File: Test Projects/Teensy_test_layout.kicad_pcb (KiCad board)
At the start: 2 copper layers, 203.2 x 101.6 mm, 106 parts, among them P1 CONN_01X02, P10 CONN_01X08, P11 CONN_01X08, P12 COLUMNS, P13 CONN_01X08, P14 CONN_01X08, P15 CONN_01X08, P16 CONN_01X08, P17 CONN_01X08, P18 CONN_01X08, P19 CONN_01X08, P2 CONN_01X07, P20 CONN_01X08, P3 CONN_01X08, P4 CONN_01X08, P5 CONN_01X08, P6 CONN_01X08, P7 ROWS, P8 CONN_01X08, P9 CONN_01X08, U1 LDO-adj-4term, U10 SF-4052, U11 SF-4052, U12 SF-4052, U13 SF-4052, U14 SF-4052, U15 SF-4052, U16 SF-4052, U17 SF-4052, U18 SF-74HC595, U19 SF-74HC595, U2 Teensy_3.2, U20 SF-74HC595, U21 SF-74HC595, U22 SF-74HC595, U23 SF-74HC595, U24 SF-74HC595, U25 SF-74HC595, U26 SF-74HC595, U27 SF-74HC595, U3 LDO-adj-4term, U4 SGTL5000, U5 SF-MicroSD-12term, U6 LDO-adj-4term, U7 2N168, U8 SF-4052, U9 SF-4052

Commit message: Tested a few layout sections
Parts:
- removed JACK1: TRS_6term, SparkFun-Footprints:SF-Neutrik-Jack-6-term
- moved C12 16.1 mm to (85.7, 131.7), turned to 270 degrees
- moved R5 15.0 mm to (130.5, 77.1)
- moved C10 15.0 mm to (130.5, 73.3)
- moved C9 15.0 mm to (128.0, 73.3)
- moved JMP4 15.0 mm to (133.9, 64.4)
- moved JMP1 15.0 mm to (114.4, 86.0)
- moved JMP2 15.0 mm to (114.4, 79.6)
- moved R6 15.0 mm to (122.9, 84.7)
- moved R7 15.0 mm to (119.1, 84.7)
- moved C11 15.0 mm to (125.2, 65.6)
- moved C8 15.0 mm to (122.9, 78.3)
- moved C7 15.0 mm to (115.3, 72.0)
- moved JMP3 15.0 mm to (128.8, 79.6)
- moved U4 15.0 mm to (122.0, 72.4)
- moved U16 14.8 mm to (193.5, 76.7)
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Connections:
- net Net-(C1-Pad1) renamed /page1/Bulk_IN
- U10 pad 13: (no net) -> KOUT5
- U10 pad 3: (no net) -> KOUT6
- U11 pad 13: (no net) -> KOUT7
- U11 pad 3: (no net) -> KOUT8
- U16 pad 1: (no net) -> KOUT5
- U16 pad 11: (no net) -> KOUT4
- U16 pad 12: (no net) -> KOUT1
- U16 pad 14: (no net) -> KOUT2
- U16 pad 15: (no net) -> KOUT3
- U16 pad 2: (no net) -> KOUT7
- U16 pad 4: (no net) -> KOUT8
- U16 pad 5: (no net) -> KOUT6
- U18 pad 14: BSER -> LEDSER
- U2 pad 28: (no net) -> BCLK
- U2 pad 29: BCLK -> (no net)
- U2 pad 31: (no net) -> LEDSER
- U8 pad 13: (no net) -> KOUT1
- U8 pad 3: (no net) -> KOUT2
- U9 pad 13: (no net) -> KOUT3
- U9 pad 3: (no net) -> KOUT4
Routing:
- net LEDSCLK: track 0.00 -> 102.9 mm, vias 0 -> 8
- net LEDLATCH: track 0.00 -> 101.0 mm, vias 0 -> 8
- net LEDOE: track 0.00 -> 99.2 mm, vias 0 -> 8
- net B: track 0.00 -> 62.6 mm, vias 0 -> 5
- net A: track 0.00 -> 58.4 mm, vias 0 -> 5
- net KOUT8: track 0.00 -> 58.2 mm, vias 0 -> 2
- net KOUT7: track 0.00 -> 53.8 mm, vias 0 -> 2
- net KOUT6: track 0.00 -> 44.3 mm, vias 0 -> 2
- net KOUT5: track 0.00 -> 41.6 mm, vias 0 -> 2
- net KOUT1: track 0.00 -> 30.2 mm, vias 0 -> 2
- net K17: track 0.00 -> 27.1 mm
- net KOUT2: track 0.00 -> 26.8 mm, vias 0 -> 2
- net K1: track 0.00 -> 26.4 mm
- net K4: track 0.00 -> 23.7 mm, vias 0 -> 2
- net K20: track 0.00 -> 22.9 mm, vias 0 -> 1
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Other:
- net class Default: clearance 0.2 -> 0.1778; trace_width 0.25 -> 0.1778; via_dia 0.6 -> 0.635; via_drill 0.4 -> 0.381
- net class JackLine added: clearance 0.3048, trace_width 0.3048, via_dia 0.635, via_drill 0.381
- net class Power added: clearance 0.254, trace_width 0.4064, via_dia 0.635, via_drill 0.381
- net class Signal added: clearance 0.254, trace_width 0.2032, via_dia 0.635, via_drill 0.381
- rule trace_clearance: 0.2 -> 0.1778
- rule trace_min: 0.2 -> 0.1778
- rule via_min_drill: 0.3 -> 0.381
- rule via_min_size: 0.4 -> 0.508

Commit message: Continued proto 1 layout
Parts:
- added C36: C, Capacitors_Tantalum_SMD:TantalC_SizeB_EIA-3528_Reflow, F.Cu at (176.3, 87.6)
- added P21: CONN_01X03, Pin_Headers:Pin_Header_Straight_1x03, F.Cu at (153.7, 90.2)
- added P2101: CONN_01X05, Pin_Headers:Pin_Header_Straight_1x05, F.Cu at (154.9, 69.8)
- added P211: CONN_01X05, Pin_Headers:Pin_Header_Straight_1x05, F.Cu at (132.1, 69.8)
- added P211: CONN_01X06, Pin_Headers:Pin_Header_Straight_1x06, F.Cu at (152.4, 63.5)
- added P211: CONN_01X06, Pin_Headers:Pin_Header_Straight_1x06, F.Cu at (172.7, 63.5)
- added P2111: CONN_01X05, Pin_Headers:Pin_Header_Straight_1x05, F.Cu at (157.5, 69.8)
- added P2121: CONN_01X05, Pin_Headers:Pin_Header_Straight_1x05, F.Cu at (160.0, 69.8)
- added P2131: CONN_01X05, Pin_Headers:Pin_Header_Straight_1x05, F.Cu at (162.6, 69.8)
- added P2141: CONN_01X05, Pin_Headers:Pin_Header_Straight_1x05, F.Cu at (165.1, 69.8)
- added P2151: CONN_01X05, Pin_Headers:Pin_Header_Straight_1x05, F.Cu at (167.6, 69.8)
- added P2161: CONN_01X05, Pin_Headers:Pin_Header_Straight_1x05, F.Cu at (170.2, 69.8)
- added P2171: CONN_01X05, Pin_Headers:Pin_Header_Straight_1x05, F.Cu at (172.7, 69.8)
- added P2181: CONN_01X05, Pin_Headers:Pin_Header_Straight_1x05, F.Cu at (175.3, 69.8)
- added P2191: CONN_01X05, Pin_Headers:Pin_Header_Straight_1x05, F.Cu at (177.8, 69.8)
- added P22: CONN_01X05, Pin_Headers:Pin_Header_Straight_1x05, F.Cu at (66.0, 95.2)
- added P2201: CONN_01X05, Pin_Headers:Pin_Header_Straight_1x05, F.Cu at (180.3, 69.8)
- added P221: CONN_01X05, Pin_Headers:Pin_Header_Straight_1x05, F.Cu at (134.6, 69.8)
- added P2211: CONN_01X05, Pin_Headers:Pin_Header_Straight_1x05, F.Cu at (182.9, 69.8)
- added P2221: CONN_01X05, Pin_Headers:Pin_Header_Straight_1x05, F.Cu at (185.4, 69.8)
- added P2231: CONN_01X05, Pin_Headers:Pin_Header_Straight_1x05, F.Cu at (188.0, 74.9)
- added P2241: CONN_01X05, Pin_Headers:Pin_Header_Straight_1x05, F.Cu at (188.0, 72.4)
- added P2251: CONN_01X05, Pin_Headers:Pin_Header_Straight_1x05, F.Cu at (188.0, 69.8)
- added P23: CONN_01X05, Pin_Headers:Pin_Header_Straight_1x05, F.Cu at (68.6, 95.2)
- added P231: CONN_01X05, Pin_Headers:Pin_Header_Straight_1x05, F.Cu at (137.2, 69.8)
- added P24: CONN_01X05, Pin_Headers:Pin_Header_Straight_1x05, F.Cu at (71.1, 95.2)
- added P241: CONN_01X05, Pin_Headers:Pin_Header_Straight_1x05, F.Cu at (139.7, 69.8)
- added P25: CONN_01X05, Pin_Headers:Pin_Header_Straight_1x05, F.Cu at (73.7, 95.2)
- added P251: CONN_01X05, Pin_Headers:Pin_Header_Straight_1x05, F.Cu at (142.2, 69.8)
- added P26: CONN_01X05, Pin_Headers:Pin_Header_Straight_1x05, F.Cu at (76.2, 95.2)
- added P261: CONN_01X05, Pin_Headers:Pin_Header_Straight_1x05, F.Cu at (144.8, 69.8)
- added P27: CONN_01X06, Pin_Headers:Pin_Header_Straight_1x06, F.Cu at (132.1, 63.5)
- added P271: CONN_01X05, Pin_Headers:Pin_Header_Straight_1x05, F.Cu at (147.3, 69.8)
- added P281: CONN_01X05, Pin_Headers:Pin_Header_Straight_1x05, F.Cu at (149.9, 69.8)
- added P291: CONN_01X05, Pin_Headers:Pin_Header_Straight_1x05, F.Cu at (152.4, 69.8)
- added P311: CONN_01X06, Pin_Headers:Pin_Header_Straight_1x06, F.Cu at (193.0, 63.5)
- added P311: CONN_01X06, Pin_Headers:Pin_Header_Straight_1x06, F.Cu at (213.4, 63.5)
- added P311: CONN_01X06, Pin_Headers:Pin_Header_Straight_1x06, F.Cu at (233.7, 63.5)
- added R11: R, Resistors_SMD:R_0603, F.Cu at (90.2, 58.4)
- added R12: R, Resistors_SMD:R_0603, F.Cu at (110.5, 58.4)
- added R13: R, Resistors_SMD:R_0603, F.Cu at (97.8, 58.4)
- added R14: R, Resistors_SMD:R_0603, F.Cu at (118.1, 58.4)
- added R15: R, Resistors_SMD:R_0603, F.Cu at (86.4, 68.6)
- added U28: SF-74x125, SparkFun-Footprints:SF-SOT-23-5, F.Cu at (94.0, 59.9)
- added U29: SF-74x125, SparkFun-Footprints:SF-SOT-23-5, F.Cu at (114.3, 59.7)
- added U30: SF-LM358, SparkFun-Footprints:SF-SOIC-8, F.Cu at (177.2, 88.3)
- P12: value COLUMNS -> COLS1
- P7: value ROWS -> COLS0
- moved JMP4 35.6 mm to (160.8, 87.6)
- moved C4 34.7 mm to (103.1, 83.8)
- moved C6 34.7 mm to (108.0, 92.7)
- moved R3 34.7 mm to (117.6, 86.4)
- moved R4 34.7 mm to (116.8, 91.4)
- moved C5 34.7 mm to (121.9, 88.9)
- moved U6 34.7 mm to (110.5, 84.4)
- moved U2 34.4 mm to (170.2, 119.4), turned to 180 degrees
- moved C10 33.5 mm to (157.2, 93.6)
- moved C9 33.5 mm to (154.6, 93.6)
- moved R5 33.5 mm to (157.2, 97.4)
- moved C11 33.5 mm to (151.9, 86.0)
- moved C8 33.5 mm to (149.6, 98.7)
- moved JMP1 33.5 mm to (141.1, 106.3)
- moved JMP2 33.5 mm to (141.1, 99.9)
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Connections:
- C26 pad 1: Net-(C26-Pad1) -> +5V
- C26 pad 2: Net-(C26-Pad2) -> GND
- C27 pad 1: Net-(C27-Pad1) -> +5V
- C27 pad 2: Net-(C27-Pad2) -> GND
- C28 pad 1: Net-(C28-Pad1) -> +5V
- C28 pad 2: Net-(C28-Pad2) -> GND
- C29 pad 1: Net-(C29-Pad1) -> +5V
- C29 pad 2: Net-(C29-Pad2) -> GND
- C30 pad 1: Net-(C30-Pad1) -> +5V
- C30 pad 2: Net-(C30-Pad2) -> GND
- C31 pad 1: Net-(C31-Pad1) -> +5V
- C31 pad 2: Net-(C31-Pad2) -> GND
- C32 pad 1: Net-(C32-Pad1) -> +5V
- C32 pad 2: Net-(C32-Pad2) -> GND
- C33 pad 1: Net-(C33-Pad1) -> +5V
- C33 pad 2: Net-(C33-Pad2) -> GND
- JACK10 pad G: (no net) -> Net-(JACK10-PadG)
- JACK10 pad R: (no net) -> Net-(JACK10-PadR)
- JACK10 pad RN: (no net) -> Net-(JACK10-PadRN)
- JACK10 pad S: (no net) -> Net-(JACK10-PadS)
- JACK10 pad T: (no net) -> Net-(JACK10-PadT)
- JACK10 pad TN: (no net) -> Net-(JACK10-PadTN)
- JACK3 pad 4: (no net) -> Net-(JACK3-Pad4)
- JACK3 pad 5: (no net) -> Net-(JACK3-Pad5)
- JACK4 pad 4: (no net) -> Net-(JACK4-Pad4)
- JACK4 pad 5: (no net) -> Net-(JACK4-Pad5)
- JACK5 pad G: (no net) -> Net-(JACK5-PadG)
- JACK5 pad R: (no net) -> Net-(JACK5-PadR)
- JACK5 pad RN: (no net) -> Net-(JACK5-PadRN)
- JACK5 pad S: (no net) -> Net-(JACK5-PadS)
- JACK5 pad T: (no net) -> Net-(JACK5-PadT)
- JACK5 pad TN: (no net) -> Net-(JACK5-PadTN)
- JACK6 pad G: (no net) -> Net-(JACK6-PadG)
- JACK6 pad R: (no net) -> Net-(JACK6-PadR)
- JACK6 pad RN: (no net) -> Net-(JACK6-PadRN)
- JACK6 pad S: (no net) -> Net-(JACK6-PadS)
- JACK6 pad T: (no net) -> Net-(JACK6-PadT)
- JACK6 pad TN: (no net) -> Net-(JACK6-PadTN)
- JACK7 pad G: (no net) -> Net-(JACK7-PadG)
- JACK7 pad R: (no net) -> Net-(JACK7-PadR)
- JACK7 pad RN: (no net) -> Net-(JACK7-PadRN)
- JACK7 pad S: (no net) -> Net-(JACK7-PadS)
- JACK7 pad T: (no net) -> Net-(JACK7-PadT)
- JACK7 pad TN: (no net) -> Net-(JACK7-PadTN)
- JACK8 pad G: (no net) -> Net-(JACK8-PadG)
- JACK8 pad R: (no net) -> Net-(JACK8-PadR)
- JACK8 pad RN: (no net) -> Net-(JACK8-PadRN)
- JACK8 pad S: (no net) -> Net-(JACK8-PadS)
- JACK8 pad T: (no net) -> Net-(JACK8-PadT)
- JACK8 pad TN: (no net) -> Net-(JACK8-PadTN)
- JACK9 pad G: (no net) -> Net-(JACK9-PadG)
- JACK9 pad R: (no net) -> Net-(JACK9-PadR)
- JACK9 pad RN: (no net) -> Net-(JACK9-PadRN)
- JACK9 pad S: (no net) -> Net-(JACK9-PadS)
- JACK9 pad T: (no net) -> Net-(JACK9-PadT)
- JACK9 pad TN: (no net) -> Net-(JACK9-PadTN)
- P2 pad 5: (no net) -> KEN
- U18 pad 16: Net-(C26-Pad1) -> +5V
- U18 pad 8: Net-(C26-Pad2) -> GND
- U19 pad 16: Net-(C27-Pad1) -> +5V
- U19 pad 8: Net-(C27-Pad2) -> GND
- U2 pad 21: (no net) -> KEN
- U20 pad 16: Net-(C28-Pad1) -> +5V
- U20 pad 8: Net-(C28-Pad2) -> GND
- U21 pad 16: Net-(C29-Pad1) -> +5V
- U21 pad 8: Net-(C29-Pad2) -> GND
- U22 pad 16: Net-(C30-Pad1) -> +5V
- U22 pad 8: Net-(C30-Pad2) -> GND
- U23 pad 16: Net-(C31-Pad1) -> +5V
- U23 pad 8: Net-(C31-Pad2) -> GND
- U24 pad 16: Net-(C32-Pad1) -> +5V
- U24 pad 8: Net-(C32-Pad2) -> GND
- U25 pad 16: Net-(C33-Pad1) -> +5V
- U25 pad 8: Net-(C33-Pad2) -> GND
- U7 pad 5: (no net) -> GND
- U7 pad 6: (no net) -> PORT-TX
- U7 pad 8: (no net) -> +5V
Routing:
- net Net-(C29-Pad2): track 1.94 -> 0.00 mm
- net GND: track 13.6 -> 15.5 mm
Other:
- board size 203.2 x 101.6 mm -> 190.5 x 101.6 mm

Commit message: Moved to 10x5 size
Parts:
- removed P2101, P211, P2111, P2121, P2131, P2141, P2151, P2161, P2171, P2181, P2191, P2201, P221, P2211, P2221, P2231, P2241, P2251, P231, P241, P251, P261, P271, P281, P291: CONN_01X05, Pin_Headers:Pin_Header_Straight_1x05
- removed P211 (x2), P311 (x3): CONN_01X06, Pin_Headers:Pin_Header_Straight_1x06
- added JACK1: DIN-5, SparkFun-Footprints:SF-DIN-5, F.Cu at (58.4, 25.4)
- added JACK11: TRS_6term, SparkFun-Footprints:SF-Neutrik-Jack-6-term, F.Cu at (264.2, 25.4)
- added P28: CONN_01X08, Pin_Headers:Pin_Header_Straight_1x08, F.Cu at (233.7, 144.8)
- added P29: CONN_01X08, Pin_Headers:Pin_Header_Straight_1x08, F.Cu at (254.0, 144.8)
- added ROWS1: CONN_01X04, Pin_Headers:Pin_Header_Straight_1x04, F.Cu at (139.7, 132.1)
- C12, C13, C14: value 10u -> C; footprint Capacitors_Tantalum_SMD:TantalC_SizeB_EIA-3528_Reflow -> Capacitors_SMD:C_1206
- C15, C36: footprint Capacitors_Tantalum_SMD:TantalC_SizeB_EIA-3528_Reflow -> Capacitors_SMD:C_0603
- C16: value 1u -> C
- C17, C18: value 1u -> C; footprint Capacitors_SMD:C_0603 -> Capacitors_Tantalum_SMD:TantalC_SizeB_EIA-3528_Reflow
- C26, C27, C28: value C -> 1u
- C7, C8, C9: value C -> 10u; footprint Capacitors_SMD:C_1206 -> Capacitors_Tantalum_SMD:TantalC_SizeB_EIA-3528_Reflow
- JACK4: value DIN-5 -> TRS_6term; footprint SparkFun-Footprints:SF-DIN-5 -> SparkFun-Footprints:SF-Neutrik-Jack-6-term
- JMP1: value 2Jumper -> 3Jumper; footprint SparkFun-Footprints:SF-2way-open -> SparkFun-Footprints:SF-3way-open
- JMP3: value 3Jumper -> 2Jumper; footprint SparkFun-Footprints:SF-3way-open -> SparkFun-Footprints:SF-2way-open
- P10, P11, P5, P6, P8, P9: value CONN_01X08 -> CONN_01X06; footprint Pin_Headers:Pin_Header_Straight_1x08 -> Pin_Headers:Pin_Header_Straight_1x06
- P12: value COLS1 -> CONN_01X06; footprint Pin_Headers:Pin_Header_Straight_1x08 -> Pin_Headers:Pin_Header_Straight_1x06
- P2: value CONN_01X07 -> CONN_01X03; footprint Pin_Headers:Pin_Header_Straight_1x07 -> Pin_Headers:Pin_Header_Straight_1x03
- P21: value CONN_01X03 -> CONN_01X07; footprint Pin_Headers:Pin_Header_Straight_1x03 -> Pin_Headers:Pin_Header_Straight_1x07
- P22, P23, P24, P25, P26: value CONN_01X05 -> CONN_01X08; footprint Pin_Headers:Pin_Header_Straight_1x05 -> Pin_Headers:Pin_Header_Straight_1x08
- P27: value CONN_01X06 -> CONN_01X08; footprint Pin_Headers:Pin_Header_Straight_1x06 -> Pin_Headers:Pin_Header_Straight_1x08
- P3: value CONN_01X08 -> COLS0
- P4: value CONN_01X08 -> COLS1
- P7: value COLS0 -> CONN_01X06; footprint Pin_Headers:Pin_Header_Straight_1x08 -> Pin_Headers:Pin_Header_Straight_1x06
- R3: value 11.5K -> 11.3K
- R4: value 18.7K -> 34K
- R5: value 1 -> 11.5K
- R6: value 2.2K -> 18.7K
- R7: value 2.2K -> 1
- R8: value 11.3K -> 2.2K
- R9: value 34K -> 2.2K
- U10, U9: value SF-4052 -> SF-74x125; footprint SparkFun-Footprints:SF-SOIC-16 -> SparkFun-Footprints:SF-SOT-23-5
- U11: value SF-4052 -> 2N168; footprint SparkFun-Footprints:SF-SOIC-16 -> SparkFun-Footprints:SF-SMD-8
- U12: value SF-4052 -> SF-LM358; footprint SparkFun-Footprints:SF-SOIC-16 -> SparkFun-Footprints:SF-SOIC-8
- U18, U19, U20, U21, U22: value SF-74HC595 -> SF-4052
- U2: value Teensy_3.2 -> LDO-adj-4term; footprint teensy footprints:Teensy_3.2_Route -> SparkFun-Footprints:SF-SOT-223
- U28, U29: value SF-74x125 -> SF-74HC595; footprint SparkFun-Footprints:SF-SOT-23-5 -> SparkFun-Footprints:SF-SOIC-16
- U3: value LDO-adj-4term -> Teensy_3.2; footprint SparkFun-Footprints:SF-SOT-223 -> teensy footprints:Teensy_3.2_Route
- U30: value SF-LM358 -> SF-74HC595; footprint SparkFun-Footprints:SF-SOIC-8 -> SparkFun-Footprints:SF-SOIC-16
- U4: value SGTL5000 -> LDO-adj-4term; footprint SparkFun-Footprints:SF-QFN-32-NXP-SGTL5000 -> SparkFun-Footprints:SF-SOT-223
- U5: value SF-MicroSD-12term -> SGTL5000; footprint SparkFun-Footprints:SF-MICRO-SD -> SparkFun-Footprints:SF-QFN-32-NXP-SGTL5000
- U6: value LDO-adj-4term -> SF-MicroSD-12term; footprint SparkFun-Footprints:SF-SOT-223 -> SparkFun-Footprints:SF-MICRO-SD
- U7: value 2N168 -> SF-74HC595; footprint SparkFun-Footprints:SF-SMD-8 -> SparkFun-Footprints:SF-SOIC-16
- U8: value SF-4052 -> SF-74HC595
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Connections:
- C10 pad 1: Net-(C10-Pad1) -> +3V3
- C11 pad 1: Net-(C11-Pad1) -> +1V8
- C12 pad 1: /page1/Bulk_IN -> Net-(C12-Pad1)
- C13 pad 1: +1V8 -> Net-(C12-Pad1)
- C16 pad 1: VDD -> Net-(C16-Pad1)
- C16 pad 2: GND -> Net-(C16-Pad2)
- C17 pad 1: VDD -> Net-(C17-Pad1)
- C17 pad 2: GND -> Net-(C17-Pad2)
- C18 pad 1: VDD -> GND
- C18 pad 2: GND -> +5V
- C2 pad 1: +5V -> +1V8
- C26 pad 1: +5V -> VDD
- C27 pad 1: +5V -> VDD
- C28 pad 1: +5V -> VDD
- C34 pad 1: Net-(C34-Pad1) -> +5V
- C34 pad 2: Net-(C34-Pad2) -> GND
- C35 pad 1: Net-(C35-Pad1) -> +5V
- C35 pad 2: Net-(C35-Pad2) -> GND
- C36 pad 1: GND -> +5V
- C36 pad 2: +5V -> GND
- C5 pad 1: Net-(C5-Pad1) -> +5V
- C7 pad 1: +3V3 -> /page1/Bulk_IN
- C8 pad 1: +1V8 -> Net-(C8-Pad1)
- C9 pad 1: Net-(C10-Pad1) -> Net-(C9-Pad1)
- JACK2 pad 4: Net-(C15-Pad2) -> Net-(JACK2-Pad4)
- JACK2 pad 5: Net-(C15-Pad1) -> Net-(JACK2-Pad5)
- JACK3 pad 4: Net-(JACK3-Pad4) -> Net-(C17-Pad2)
- JACK3 pad 5: Net-(JACK3-Pad5) -> Net-(C17-Pad1)
- JMP1 pad 1: PIN22 -> Net-(JMP1-Pad1)
- JMP1 pad 2: Net-(JMP1-Pad2) -> +3V3
- JMP2 pad 1: PIN13 -> I2S_DIN
- JMP3 pad 1: GND -> I2S_DOUT
- JMP4 pad 1: Net-(JMP4-Pad1) -> GND
- JMP4 pad 2: +3V3 -> Net-(JMP4-Pad2)
- JMP4 pad 3: Net-(C5-Pad1) -> +3V3
- P10 pad 1: K49 -> Net-(JACK9-PadT)
- P10 pad 2: K50 -> Net-(JACK9-PadR)
- P10 pad 3: K51 -> Net-(JACK9-PadS)
- P10 pad 4: K52 -> Net-(JACK9-PadG)
- P10 pad 5: K53 -> Net-(JACK9-PadRN)
- P10 pad 6: K54 -> Net-(JACK9-PadTN)
- P11 pad 1: K57 -> Net-(JACK10-PadT)
- P11 pad 2: K58 -> Net-(JACK10-PadR)
- P11 pad 3: K59 -> Net-(JACK10-PadS)
- P11 pad 4: K60 -> Net-(JACK10-PadG)
- P11 pad 5: K61 -> Net-(JACK10-PadRN)
- P11 pad 6: K62 -> Net-(JACK10-PadTN)
- P12 pad 1: Net-(P12-Pad1) -> Net-(JACK11-PadT)
- P12 pad 2: Net-(P12-Pad2) -> Net-(JACK11-PadR)
- P12 pad 3: Net-(P12-Pad3) -> Net-(JACK11-PadS)
- P12 pad 4: Net-(P12-Pad4) -> Net-(JACK11-PadG)
- P12 pad 5: Net-(P12-Pad5) -> Net-(JACK11-PadRN)
- P12 pad 6: Net-(P12-Pad6) -> Net-(JACK11-PadTN)
- P13 pad 1: Net-(P13-Pad1) -> K1
- P13 pad 2: Net-(P13-Pad2) -> K2
- P13 pad 3: Net-(P13-Pad3) -> K3
- P13 pad 4: Net-(P13-Pad4) -> K4
- P13 pad 5: Net-(P13-Pad5) -> K5
- P13 pad 6: Net-(P13-Pad6) -> K6
- P13 pad 7: Net-(P13-Pad7) -> K7
- P13 pad 8: Net-(P13-Pad8) -> K8
- P14 pad 1: Net-(P14-Pad1) -> K9
- P14 pad 2: Net-(P14-Pad2) -> K10
- P14 pad 3: Net-(P14-Pad3) -> K11
- P14 pad 4: Net-(P14-Pad4) -> K12
- P14 pad 5: Net-(P14-Pad5) -> K13
- P14 pad 6: Net-(P14-Pad6) -> K14
- P14 pad 7: Net-(P14-Pad7) -> K15
- P14 pad 8: Net-(P14-Pad8) -> K16
- P15 pad 1: Net-(P15-Pad1) -> K17
- P15 pad 2: Net-(P15-Pad2) -> K18
- P15 pad 3: Net-(P15-Pad3) -> K19
- P15 pad 4: Net-(P15-Pad4) -> K20
- P15 pad 5: Net-(P15-Pad5) -> K21
- P15 pad 6: Net-(P15-Pad6) -> K22
- P15 pad 7: Net-(P15-Pad7) -> K23
- P15 pad 8: Net-(P15-Pad8) -> K24
- P16 pad 1: Net-(P16-Pad1) -> K25
- P16 pad 2: Net-(P16-Pad2) -> K26
- P16 pad 3: Net-(P16-Pad3) -> K27
- P16 pad 4: Net-(P16-Pad4) -> K28
- P16 pad 5: Net-(P16-Pad5) -> K29
- P16 pad 6: Net-(P16-Pad6) -> K30
- P16 pad 7: Net-(P16-Pad7) -> K31
- P16 pad 8: Net-(P16-Pad8) -> K32
- P17 pad 1: Net-(P17-Pad1) -> K33
- P17 pad 2: Net-(P17-Pad2) -> K34
- P17 pad 3: Net-(P17-Pad3) -> K35
- P17 pad 4: Net-(P17-Pad4) -> K36
- P17 pad 5: Net-(P17-Pad5) -> K37
- P17 pad 6: Net-(P17-Pad6) -> K38
- P17 pad 7: Net-(P17-Pad7) -> K39
- P17 pad 8: Net-(P17-Pad8) -> K40
- P18 pad 1: Net-(P18-Pad1) -> K41
- P18 pad 2: Net-(P18-Pad2) -> K42
- P18 pad 3: Net-(P18-Pad3) -> K43
- P18 pad 4: Net-(P18-Pad4) -> K44
- P18 pad 5: Net-(P18-Pad5) -> K45
- P18 pad 6: Net-(P18-Pad6) -> K46
- P18 pad 7: Net-(P18-Pad7) -> K47
- P18 pad 8: Net-(P18-Pad8) -> K48
- P19 pad 1: Net-(P19-Pad1) -> K49
- P19 pad 2: Net-(P19-Pad2) -> K50
- P19 pad 3: Net-(P19-Pad3) -> K51
- P19 pad 4: Net-(P19-Pad4) -> K52
- P19 pad 5: Net-(P19-Pad5) -> K53
- P19 pad 6: Net-(P19-Pad6) -> K54
- P19 pad 7: Net-(P19-Pad7) -> K55
- P19 pad 8: Net-(P19-Pad8) -> K56
- P2 pad 1: KA0 -> Net-(P2-Pad1)
- P2 pad 2: KA1 -> Net-(P2-Pad2)
- P2 pad 3: KA2 -> Net-(P2-Pad3)
- P20 pad 1: Net-(P20-Pad1) -> K57
- P20 pad 2: Net-(P20-Pad2) -> K58
- P20 pad 3: Net-(P20-Pad3) -> K59
- P20 pad 4: Net-(P20-Pad4) -> K60
- P20 pad 5: Net-(P20-Pad5) -> K61
- P20 pad 6: Net-(P20-Pad6) -> K62
- P20 pad 7: Net-(P20-Pad7) -> K63
- P20 pad 8: Net-(P20-Pad8) -> K64
- P21 pad 1: Net-(P21-Pad1) -> KA0
- P21 pad 2: Net-(P21-Pad2) -> KA1
- P21 pad 3: Net-(P21-Pad3) -> KA2
- P22 pad 1: (no net) -> Net-(P22-Pad1)
- P22 pad 2: (no net) -> Net-(P22-Pad2)
- P22 pad 3: (no net) -> Net-(P22-Pad3)
- P22 pad 4: (no net) -> Net-(P22-Pad4)
- P22 pad 5: (no net) -> Net-(P22-Pad5)
- P23 pad 1: (no net) -> Net-(P23-Pad1)
- P23 pad 2: (no net) -> Net-(P23-Pad2)
- P23 pad 3: (no net) -> Net-(P23-Pad3)
- P23 pad 4: (no net) -> Net-(P23-Pad4)
- P23 pad 5: (no net) -> Net-(P23-Pad5)
- P24 pad 1: (no net) -> Net-(P24-Pad1)
- P24 pad 2: (no net) -> Net-(P24-Pad2)
- P24 pad 3: (no net) -> Net-(P24-Pad3)
- P24 pad 4: (no net) -> Net-(P24-Pad4)
- P24 pad 5: (no net) -> Net-(P24-Pad5)
- P25 pad 1: (no net) -> Net-(P25-Pad1)
- P25 pad 2: (no net) -> Net-(P25-Pad2)
- P25 pad 3: (no net) -> Net-(P25-Pad3)
- P25 pad 4: (no net) -> Net-(P25-Pad4)
- P25 pad 5: (no net) -> Net-(P25-Pad5)
- P26 pad 1: (no net) -> Net-(P26-Pad1)
- P26 pad 2: (no net) -> Net-(P26-Pad2)
- P26 pad 3: (no net) -> Net-(P26-Pad3)
- P26 pad 4: (no net) -> Net-(P26-Pad4)
- P26 pad 5: (no net) -> Net-(P26-Pad5)
- P27 pad 1: Net-(JACK5-PadRN) -> Net-(P27-Pad1)
- P27 pad 2: Net-(JACK5-PadR) -> Net-(P27-Pad2)
- P27 pad 3: Net-(JACK5-PadTN) -> Net-(P27-Pad3)
- P27 pad 4: Net-(JACK5-PadT) -> Net-(P27-Pad4)
- P27 pad 5: Net-(JACK5-PadG) -> Net-(P27-Pad5)
- P27 pad 6: Net-(JACK5-PadS) -> Net-(P27-Pad6)
- P3 pad 1: K1 -> Net-(P3-Pad1)
- P3 pad 2: K2 -> Net-(P3-Pad2)
- P3 pad 3: K3 -> Net-(P3-Pad3)
- P3 pad 4: K4 -> Net-(P3-Pad4)
- P3 pad 5: K5 -> Net-(P3-Pad5)
- P3 pad 6: K6 -> Net-(P3-Pad6)
- P3 pad 7: K7 -> Net-(P3-Pad7)
- P3 pad 8: K8 -> Net-(P3-Pad8)
- P4 pad 1: K9 -> Net-(P4-Pad1)
- P4 pad 2: K10 -> Net-(P4-Pad2)
- P4 pad 3: K11 -> Net-(P4-Pad3)
- P4 pad 4: K12 -> Net-(P4-Pad4)
- P4 pad 5: K13 -> Net-(P4-Pad5)
- P4 pad 6: K14 -> Net-(P4-Pad6)
- P4 pad 7: K15 -> Net-(P4-Pad7)
- P4 pad 8: K16 -> Net-(P4-Pad8)
- P5 pad 1: K17 -> Net-(JACK4-PadT)
- P5 pad 2: K18 -> Net-(JACK4-PadR)
- P5 pad 3: K19 -> Net-(JACK4-PadS)
- P5 pad 4: K20 -> Net-(JACK4-PadG)
- P5 pad 5: K21 -> Net-(JACK4-PadRN)
- P5 pad 6: K22 -> Net-(JACK4-PadTN)
- P6 pad 1: K25 -> Net-(JACK5-PadT)
- P6 pad 2: K26 -> Net-(JACK5-PadR)
- P6 pad 3: K27 -> Net-(JACK5-PadS)
- P6 pad 4: K28 -> Net-(JACK5-PadG)
- P6 pad 5: K29 -> Net-(JACK5-PadRN)
- P6 pad 6: K30 -> Net-(JACK5-PadTN)
- P7 pad 1: Net-(P7-Pad1) -> Net-(JACK6-PadT)
- P7 pad 2: Net-(P7-Pad2) -> Net-(JACK6-PadR)
- P7 pad 3: Net-(P7-Pad3) -> Net-(JACK6-PadS)
- P7 pad 4: Net-(P7-Pad4) -> Net-(JACK6-PadG)
- P7 pad 5: Net-(P7-Pad5) -> Net-(JACK6-PadRN)
- P7 pad 6: Net-(P7-Pad6) -> Net-(JACK6-PadTN)
- P8 pad 1: K33 -> Net-(JACK7-PadT)
- P8 pad 2: K34 -> Net-(JACK7-PadR)
- P8 pad 3: K35 -> Net-(JACK7-PadS)
- P8 pad 4: K36 -> Net-(JACK7-PadG)
- P8 pad 5: K37 -> Net-(JACK7-PadRN)
- P8 pad 6: K38 -> Net-(JACK7-PadTN)
- P9 pad 1: K41 -> Net-(JACK8-PadT)
- P9 pad 2: K42 -> Net-(JACK8-PadR)
- P9 pad 3: K43 -> Net-(JACK8-PadS)
- P9 pad 4: K44 -> Net-(JACK8-PadG)
- P9 pad 5: K45 -> Net-(JACK8-PadRN)
- P9 pad 6: K46 -> Net-(JACK8-PadTN)
- R1 pad 1: +5V -> +1V8
- R10 pad 1: Net-(C15-Pad2) -> +5V
- R10 pad 2: Net-(R10-Pad2) -> Net-(JACK1-Pad4)
- R11 pad 2: Net-(JACK3-Pad4) -> Net-(JACK2-Pad4)
- R12 pad 1: +5V -> Net-(JACK1-Pad5)
- R12 pad 2: Net-(JACK4-Pad4) -> Net-(R12-Pad2)
- R13 pad 1: Net-(JACK3-Pad5) -> Net-(JACK2-Pad5)
- R14 pad 1: Net-(JACK4-Pad5) -> Net-(C17-Pad2)
- R15 pad 2: PORT-TX -> PORT-RX
- R3 pad 1: Net-(C5-Pad1) -> +5V
- R5 pad 1: +3V3 -> Net-(C8-Pad1)
- R5 pad 2: Net-(C10-Pad1) -> Net-(C9-Pad1)
- R6 pad 1: +3V3 -> Net-(C9-Pad1)
- R6 pad 2: SCL0 -> GND
- R7 pad 2: SDA0 -> Net-(C12-Pad1)
- R8 pad 1: +1V8 -> +3V3
- R8 pad 2: Net-(C14-Pad1) -> SCL0
- R9 pad 1: Net-(C14-Pad1) -> +3V3
- R9 pad 2: GND -> SDA0
- U1 pad 1: Net-(C14-Pad1) -> Net-(C3-Pad1)
- U10 pad 1: K21 -> GND
- U10 pad 2: K23 -> PORT-TX
- U10 pad 3: KOUT6 -> GND
- U10 pad 4: K24 -> Net-(R13-Pad2)
- U10 pad 5: K22 -> +5V
- U11 pad 1: K29 -> (no net)
- U11 pad 2: K31 -> Net-(R14-Pad2)
- U11 pad 3: KOUT8 -> Net-(C17-Pad1)
- U11 pad 4: K32 -> (no net)
- U11 pad 5: K30 -> GND
- U11 pad 6: EN -> PORT-RX
- U11 pad 7: GND -> (no net)
- U11 pad 8: (no net) -> +5V
- U12 pad 1: K37 -> (no net)
- U12 pad 2: K39 -> (no net)
- U12 pad 3: KOUT10 -> (no net)
- U12 pad 4: K40 -> GND
- U12 pad 5: K38 -> (no net)
- U12 pad 6: EN -> (no net)
- U12 pad 7: GND -> (no net)
- U12 pad 8: (no net) -> +5V
- U13 pad 1: K45 -> K5
- U13 pad 11: K44 -> K4
- U13 pad 12: K41 -> K1
- U13 pad 13: KOUT11 -> KOUT1
- U13 pad 14: K42 -> K2
- U13 pad 15: K43 -> K3
- U13 pad 2: K47 -> K7
- U13 pad 3: KOUT12 -> KOUT2
- U13 pad 4: K48 -> K8
- U13 pad 5: K46 -> K6
- U14 pad 1: K53 -> K13
- U14 pad 11: K52 -> K12
- U14 pad 12: K49 -> K9
- U14 pad 13: KOUT13 -> KOUT3
- U14 pad 14: K50 -> K10
- U14 pad 15: K51 -> K11
- U14 pad 2: K55 -> K15
- U14 pad 3: KOUT14 -> KOUT4
- U14 pad 4: K56 -> K16
- U14 pad 5: K54 -> K14
- U15 pad 1: K61 -> K21
- U15 pad 11: K60 -> K20
- U15 pad 12: K57 -> K17
- U15 pad 13: KOUT15 -> KOUT5
- U15 pad 14: K58 -> K18
- U15 pad 15: K59 -> K19
- U15 pad 2: K63 -> K23
- U15 pad 3: KOUT16 -> KOUT6
- U15 pad 4: K64 -> K24
- U15 pad 5: K62 -> K22
- U16 pad 1: KOUT5 -> K29
- U16 pad 11: KOUT4 -> K28
- U16 pad 12: KOUT1 -> K25
- U16 pad 13: KA0 -> KOUT7
- U16 pad 14: KOUT2 -> K26
- U16 pad 15: KOUT3 -> K27
- U16 pad 2: KOUT7 -> K31
- U16 pad 3: KA1 -> KOUT8
- U16 pad 4: KOUT8 -> K32
- U16 pad 5: KOUT6 -> K30
- U17 pad 1: KOUT13 -> K37
- U17 pad 11: KOUT12 -> K36
- U17 pad 12: KOUT9 -> K33
- U17 pad 13: KA2 -> KOUT9
- U17 pad 14: KOUT10 -> K34
- U17 pad 15: KOUT11 -> K35
- U17 pad 2: KOUT15 -> K39
- U17 pad 3: KA3 -> KOUT10
- U17 pad 4: KOUT16 -> K40
- U17 pad 5: KOUT14 -> K38
- U18 pad 1: Net-(P13-Pad2) -> K45
- U18 pad 10: (no net) -> A
- U18 pad 11: LEDSCLK -> K44
- U18 pad 12: LEDLATCH -> K41
- U18 pad 13: LEDOE -> KOUT11
- U18 pad 14: LEDSER -> K42
- U18 pad 15: Net-(P13-Pad1) -> K43
- U18 pad 16: +5V -> (no net)
- U18 pad 2: Net-(P13-Pad3) -> K47
- U18 pad 3: Net-(P13-Pad4) -> KOUT12
- U18 pad 4: Net-(P13-Pad5) -> K48
- U18 pad 5: Net-(P13-Pad6) -> K46
- U18 pad 6: Net-(P13-Pad7) -> EN
- U18 pad 7: Net-(P13-Pad8) -> GND
- U18 pad 8: GND -> (no net)
- U18 pad 9: Net-(U18-Pad9) -> B
- U19 pad 1: Net-(P14-Pad2) -> K53
- U19 pad 10: (no net) -> A
- U19 pad 11: LEDSCLK -> K52
- U19 pad 12: LEDLATCH -> K49
- U19 pad 13: LEDOE -> KOUT13
- U19 pad 14: Net-(U18-Pad9) -> K50
- U19 pad 15: Net-(P14-Pad1) -> K51
- U19 pad 16: +5V -> (no net)
- U19 pad 2: Net-(P14-Pad3) -> K55
- U19 pad 3: Net-(P14-Pad4) -> KOUT14
- U19 pad 4: Net-(P14-Pad5) -> K56
- U19 pad 5: Net-(P14-Pad6) -> K54
- U19 pad 6: Net-(P14-Pad7) -> EN
- U19 pad 7: Net-(P14-Pad8) -> GND
- U19 pad 8: GND -> (no net)
- U19 pad 9: Net-(U19-Pad9) -> B
- U2 pad 1: (no net) -> Net-(C6-Pad1)
- U2 pad 2: (no net) -> +5V
- U2 pad 3: (no net) -> /page1/Bulk_IN
- U2 pad 4: (no net) -> +5V
- U20 pad 1: Net-(P15-Pad2) -> K61
- U20 pad 10: (no net) -> A
- U20 pad 11: LEDSCLK -> K60
- U20 pad 12: LEDLATCH -> K57
- U20 pad 13: LEDOE -> KOUT15
- U20 pad 14: Net-(U19-Pad9) -> K58
- U20 pad 15: Net-(P15-Pad1) -> K59
- U20 pad 16: +5V -> (no net)
- U20 pad 2: Net-(P15-Pad3) -> K63
- U20 pad 3: Net-(P15-Pad4) -> KOUT16
- U20 pad 4: Net-(P15-Pad5) -> K64
- U20 pad 5: Net-(P15-Pad6) -> K62
- U20 pad 6: Net-(P15-Pad7) -> EN
- U20 pad 7: Net-(P15-Pad8) -> GND
- U20 pad 8: GND -> (no net)
- U20 pad 9: Net-(U20-Pad9) -> B
- U21 pad 1: Net-(P16-Pad2) -> KOUT5
- U21 pad 10: (no net) -> A
- U21 pad 11: LEDSCLK -> KOUT4
- U21 pad 12: LEDLATCH -> KOUT1
- U21 pad 13: LEDOE -> KA0
- U21 pad 14: Net-(U20-Pad9) -> KOUT2
- U21 pad 15: Net-(P16-Pad1) -> KOUT3
- U21 pad 16: +5V -> (no net)
- U21 pad 2: Net-(P16-Pad3) -> KOUT7
- U21 pad 3: Net-(P16-Pad4) -> KA1
- U21 pad 4: Net-(P16-Pad5) -> KOUT8
- U21 pad 5: Net-(P16-Pad6) -> KOUT6
- U21 pad 6: Net-(P16-Pad7) -> EN
- U21 pad 7: Net-(P16-Pad8) -> GND
- U21 pad 8: GND -> (no net)
- U21 pad 9: Net-(U21-Pad9) -> B
- U22 pad 1: Net-(P17-Pad2) -> KOUT13
- U22 pad 10: (no net) -> A
- U22 pad 11: LEDSCLK -> KOUT12
- U22 pad 12: LEDLATCH -> KOUT9
- U22 pad 13: LEDOE -> KA2
- U22 pad 14: Net-(U21-Pad9) -> KOUT10
- U22 pad 15: Net-(P17-Pad1) -> KOUT11
- U22 pad 16: +5V -> (no net)
- U22 pad 2: Net-(P17-Pad3) -> KOUT15
- U22 pad 3: Net-(P17-Pad4) -> KA3
- U22 pad 4: Net-(P17-Pad5) -> KOUT16
- U22 pad 5: Net-(P17-Pad6) -> KOUT14
- U22 pad 6: Net-(P17-Pad7) -> EN
- U22 pad 7: Net-(P17-Pad8) -> GND
- U22 pad 8: GND -> (no net)
- U22 pad 9: Net-(U22-Pad9) -> B
- U23 pad 1: Net-(P18-Pad2) -> Net-(P22-Pad2)
- U23 pad 11: LEDSCLK -> SD_LED_SCK
- U23 pad 14: Net-(U22-Pad9) -> SD_LED_MOSI
- U23 pad 15: Net-(P18-Pad1) -> Net-(P22-Pad1)
- U23 pad 2: Net-(P18-Pad3) -> Net-(P22-Pad3)
- U23 pad 3: Net-(P18-Pad4) -> Net-(P22-Pad4)
- U23 pad 4: Net-(P18-Pad5) -> Net-(P22-Pad5)
- U23 pad 5: Net-(P18-Pad6) -> Net-(P22-Pad6)
- U23 pad 6: Net-(P18-Pad7) -> Net-(P22-Pad7)
- U23 pad 7: Net-(P18-Pad8) -> Net-(P22-Pad8)
- U24 pad 1: Net-(P19-Pad2) -> Net-(P23-Pad2)
- U24 pad 11: LEDSCLK -> SD_LED_SCK
- U24 pad 15: Net-(P19-Pad1) -> Net-(P23-Pad1)
- U24 pad 2: Net-(P19-Pad3) -> Net-(P23-Pad3)
- U24 pad 3: Net-(P19-Pad4) -> Net-(P23-Pad4)
- U24 pad 4: Net-(P19-Pad5) -> Net-(P23-Pad5)
- U24 pad 5: Net-(P19-Pad6) -> Net-(P23-Pad6)
- U24 pad 6: Net-(P19-Pad7) -> Net-(P23-Pad7)
- U24 pad 7: Net-(P19-Pad8) -> Net-(P23-Pad8)
- U25 pad 1: Net-(P20-Pad2) -> Net-(P24-Pad2)
- U25 pad 11: LEDSCLK -> SD_LED_SCK
- U25 pad 15: Net-(P20-Pad1) -> Net-(P24-Pad1)
- U25 pad 2: Net-(P20-Pad3) -> Net-(P24-Pad3)
- U25 pad 3: Net-(P20-Pad4) -> Net-(P24-Pad4)
- U25 pad 4: Net-(P20-Pad5) -> Net-(P24-Pad5)
- U25 pad 5: Net-(P20-Pad6) -> Net-(P24-Pad6)
- U25 pad 6: Net-(P20-Pad7) -> Net-(P24-Pad7)
- U25 pad 7: Net-(P20-Pad8) -> Net-(P24-Pad8)
- U25 pad 9: (no net) -> Net-(U25-Pad9)
- U26 pad 1: Net-(P7-Pad2) -> Net-(P25-Pad2)
- U26 pad 11: BCLK -> SD_LED_SCK
- U26 pad 12: BLATCH -> LEDLATCH
- U26 pad 13: BOE -> LEDOE
- U26 pad 14: BSER -> Net-(U25-Pad9)
- U26 pad 15: Net-(P7-Pad1) -> Net-(P25-Pad1)
- U26 pad 16: Net-(C34-Pad1) -> +5V
- U26 pad 2: Net-(P7-Pad3) -> Net-(P25-Pad3)
- U26 pad 3: Net-(P7-Pad4) -> Net-(P25-Pad4)
- U26 pad 4: Net-(P7-Pad5) -> Net-(P25-Pad5)
- U26 pad 5: Net-(P7-Pad6) -> Net-(P25-Pad6)
- U26 pad 6: Net-(P7-Pad7) -> Net-(P25-Pad7)
- U26 pad 7: Net-(P7-Pad8) -> Net-(P25-Pad8)
- U26 pad 8: Net-(C34-Pad2) -> GND
- U27 pad 1: Net-(P12-Pad2) -> Net-(P26-Pad2)
- U27 pad 11: BCLK -> SD_LED_SCK
- U27 pad 12: BLATCH -> LEDLATCH
- U27 pad 13: BOE -> LEDOE
- U27 pad 15: Net-(P12-Pad1) -> Net-(P26-Pad1)
- U27 pad 16: Net-(C35-Pad1) -> +5V
- U27 pad 2: Net-(P12-Pad3) -> Net-(P26-Pad3)
- U27 pad 3: Net-(P12-Pad4) -> Net-(P26-Pad4)
- U27 pad 4: Net-(P12-Pad5) -> Net-(P26-Pad5)
- U27 pad 5: Net-(P12-Pad6) -> Net-(P26-Pad6)
- U27 pad 6: Net-(P12-Pad7) -> Net-(P26-Pad7)
- U27 pad 7: Net-(P12-Pad8) -> Net-(P26-Pad8)
- U27 pad 8: Net-(C35-Pad2) -> GND
- U27 pad 9: (no net) -> Net-(U27-Pad9)
- U28 pad 1: GND -> Net-(P27-Pad2)
- U28 pad 2: PORT-TX -> Net-(P27-Pad3)
- U28 pad 3: GND -> Net-(P27-Pad4)
- U28 pad 4: Net-(R13-Pad2) -> Net-(P27-Pad5)
- U28 pad 5: +5V -> Net-(P27-Pad6)
- U29 pad 1: GND -> Net-(P28-Pad2)
- U29 pad 2: (no net) -> Net-(P28-Pad3)
- U29 pad 3: GND -> Net-(P28-Pad4)
- U29 pad 4: Net-(R14-Pad2) -> Net-(P28-Pad5)
- U29 pad 5: +5V -> Net-(P28-Pad6)
- U3 pad 1: Net-(C3-Pad1) -> PORT-TX
- U3 pad 2: +5V -> ROW1
- U3 pad 3: /page1/Bulk_IN -> ROW2
- U3 pad 4: +5V -> ROW3
- U30 pad 1: (no net) -> Net-(P29-Pad2)
- U30 pad 2: (no net) -> Net-(P29-Pad3)
- U30 pad 3: (no net) -> Net-(P29-Pad4)
- U30 pad 4: GND -> Net-(P29-Pad5)
- U30 pad 5: (no net) -> Net-(P29-Pad6)
- U30 pad 6: (no net) -> Net-(P29-Pad7)
- U30 pad 7: (no net) -> Net-(P29-Pad8)
- U30 pad 8: +5V -> GND
- U4 pad 1: GND -> Net-(C9-Pad1)
- U4 pad 2: Net-(P21-Pad2) -> Net-(C8-Pad1)
- U4 pad 3: GND -> /page1/Bulk_IN
- U4 pad 4: Net-(P21-Pad3) -> Net-(C8-Pad1)
- U5 pad 1: (no net) -> GND
- U5 pad 10: (no net) -> Net-(C14-Pad1)
- U5 pad 2: PIN10 -> Net-(P2-Pad2)
- U5 pad 3: PIN7 -> GND
- U5 pad 4: +3V3 -> Net-(P2-Pad3)
- U5 pad 5: PIN14 -> Net-(C12-Pad1)
- U5 pad 6: GND -> Net-(P2-Pad1)
- U5 pad 7: PIN12 -> GND
- U6 pad 1: Net-(C6-Pad1) -> (no net)
- U6 pad 2: Net-(C5-Pad1) -> SD_CS
- U6 pad 3: /page1/Bulk_IN -> SD_LED_MOSI
- U6 pad 4: Net-(C5-Pad1) -> +3V3
- U7 pad 1: (no net) -> Net-(P3-Pad2)
- U7 pad 2: Net-(R10-Pad2) -> Net-(P3-Pad3)
- U7 pad 3: Net-(C15-Pad1) -> Net-(P3-Pad4)
- U7 pad 4: (no net) -> Net-(P3-Pad5)
- U7 pad 5: GND -> Net-(P3-Pad6)
- U7 pad 6: PORT-TX -> Net-(P3-Pad7)
- U7 pad 7: (no net) -> Net-(P3-Pad8)
- U7 pad 8: +5V -> Net-(C15-Pad2)
- U8 pad 1: K5 -> Net-(P4-Pad2)
- U8 pad 10: A -> (no net)
- U8 pad 11: K4 -> BCLK
- U8 pad 12: K1 -> BLATCH
- U8 pad 13: KOUT1 -> BOE
- U8 pad 14: K2 -> (no net)
- U8 pad 15: K3 -> Net-(P4-Pad1)
- U8 pad 16: (no net) -> Net-(C16-Pad1)
- U8 pad 2: K7 -> Net-(P4-Pad3)
- U8 pad 3: KOUT2 -> Net-(P4-Pad4)
- U8 pad 4: K8 -> Net-(P4-Pad5)
- U8 pad 5: K6 -> Net-(P4-Pad6)
- U8 pad 6: EN -> Net-(P4-Pad7)
- U8 pad 7: GND -> Net-(P4-Pad8)
- U8 pad 8: (no net) -> Net-(C16-Pad2)
- U8 pad 9: B -> (no net)
- U9 pad 1: K13 -> GND
- U9 pad 2: K15 -> PORT-RX
- U9 pad 3: KOUT4 -> GND
- U9 pad 4: K16 -> Net-(R12-Pad2)
- U9 pad 5: K14 -> +5V
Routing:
- net LEDSCLK: track 102.9 -> 0.00 mm, vias 8 -> 0
- net LEDLATCH: track 101.0 -> 0.00 mm, vias 8 -> 0
- net LEDOE: track 99.2 -> 0.00 mm, vias 8 -> 0
- net B: track 62.6 -> 0.00 mm, vias 5 -> 0
- net A: track 58.4 -> 0.00 mm, vias 5 -> 0
- net KOUT8: track 58.2 -> 0.00 mm, vias 2 -> 0
- net KOUT7: track 53.8 -> 0.00 mm, vias 2 -> 0
- net KOUT6: track 44.3 -> 0.00 mm, vias 2 -> 0
- net KOUT5: track 41.6 -> 0.00 mm, vias 2 -> 0
- net KOUT1: track 30.2 -> 0.00 mm, vias 2 -> 0
- net K17: track 27.1 -> 0.00 mm
- net KOUT2: track 26.8 -> 0.00 mm, vias 2 -> 0
- net K1: track 26.4 -> 0.00 mm
- net K4: track 23.7 -> 0.00 mm, vias 2 -> 0
- net K20: track 22.9 -> 0.00 mm, vias 1 -> 0
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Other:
- board size 190.5 x 101.6 mm -> 304.8 x 177.8 mm

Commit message: unfolded connectors
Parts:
- moved C15 104.1 mm to (51.5, 129.5)
- moved P3 104.1 mm to (40.6, 144.8)
- moved U8 104.1 mm to (66.0, 137.2)
- moved C16 104.1 mm to (61.0, 128.8)
- moved P4 104.1 mm to (61.0, 144.8)
- moved U7 104.1 mm to (53.3, 137.2)
- moved U3 103.1 mm to (52.1, 109.2), turned to 90 degrees
- moved ROWS1 99.1 mm to (40.6, 129.5), turned to 90 degrees
- moved C22 83.8 mm to (175.3, 114.3)
- moved U16 83.8 mm to (182.9, 111.8)
- moved C19 83.8 mm to (114.3, 114.3)
- moved C20 83.8 mm to (134.6, 114.3)
- moved C21 83.8 mm to (154.9, 114.3)
- moved P14 83.8 mm to (132.1, 119.4)
- moved P15 83.8 mm to (152.4, 119.4)
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
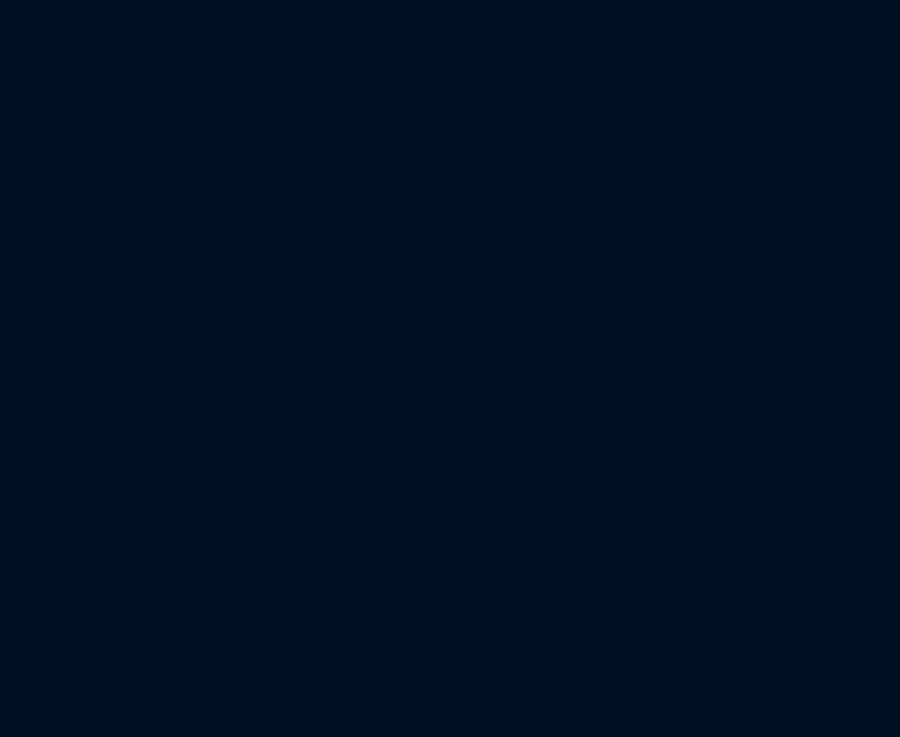
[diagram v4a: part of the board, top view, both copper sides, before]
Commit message: added second codec
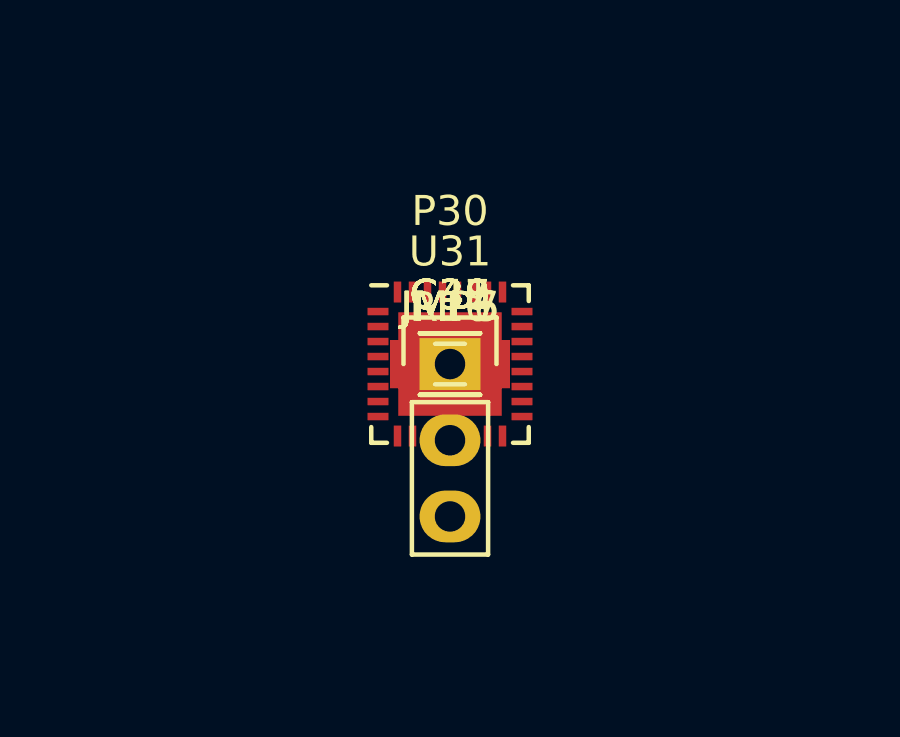
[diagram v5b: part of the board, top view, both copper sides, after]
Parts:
- added C37, C38, C39, C40, C41: C, Capacitors_SMD:C_1206, F.Cu at (109.1, 78.9)
- added JMP5: 3Jumper, SparkFun-Footprints:SF-3way-open, F.Cu at (109.1, 78.9)
- added JMP6, JMP7: 2Jumper, SparkFun-Footprints:SF-2way-open, F.Cu at (109.1, 78.9)
- added P30: CONN_01X03, Pin_Headers:Pin_Header_Straight_1x03, F.Cu at (109.1, 78.9)
- added R16: 1, Resistors_SMD:R_0603, F.Cu at (109.1, 78.9)
- added U31: SGTL5000, SparkFun-Footprints:SF-QFN-32-NXP-SGTL5000, F.Cu at (109.1, 78.9)
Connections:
- net I2S_DIN renamed I2S_DIN0
- net I2S_DOUT renamed I2S_DOUT0
- JACK1 pad 1: (no net) -> Net-(JACK1-Pad1)
- JACK1 pad 2: (no net) -> Net-(JACK1-Pad2)
- JACK1 pad 3: (no net) -> Net-(JACK1-Pad3)
- JACK1 pad 6: (no net) -> Net-(JACK1-Pad6)
- JACK1 pad 7: (no net) -> Net-(JACK1-Pad7)
- JACK2 pad 1: (no net) -> Net-(JACK2-Pad1)
- JACK2 pad 2: (no net) -> Net-(JACK2-Pad2)
- JACK2 pad 3: (no net) -> Net-(JACK2-Pad3)
- JACK2 pad 6: (no net) -> Net-(JACK2-Pad6)
- JACK2 pad 7: (no net) -> Net-(JACK2-Pad7)
- JACK3 pad 1: (no net) -> Net-(JACK3-Pad1)
- JACK3 pad 2: (no net) -> Net-(JACK3-Pad2)
- JACK3 pad 3: (no net) -> Net-(JACK3-Pad3)
- JACK3 pad 6: (no net) -> Net-(JACK3-Pad6)
- JACK3 pad 7: (no net) -> Net-(JACK3-Pad7)
- U11 pad 1: (no net) -> Net-(U11-Pad1)
- U11 pad 4: (no net) -> Net-(U11-Pad4)
- U11 pad 7: (no net) -> Net-(U11-Pad7)
- U12 pad 1: (no net) -> Net-(U12-Pad1)
- U12 pad 2: (no net) -> Net-(U12-Pad2)
- U12 pad 3: (no net) -> Net-(U12-Pad3)
- U12 pad 5: (no net) -> Net-(U12-Pad5)
- U12 pad 6: (no net) -> Net-(U12-Pad6)
- U12 pad 7: (no net) -> Net-(U12-Pad7)
- U13 pad 16: (no net) -> Net-(U13-Pad16)
- U13 pad 8: (no net) -> Net-(U13-Pad8)
- U14 pad 16: (no net) -> Net-(U14-Pad16)
- U14 pad 8: (no net) -> Net-(U14-Pad8)
- U15 pad 16: (no net) -> Net-(U15-Pad16)
- U15 pad 8: (no net) -> Net-(U15-Pad8)
- U16 pad 16: (no net) -> Net-(U16-Pad16)
- U16 pad 8: (no net) -> Net-(U16-Pad8)
- U17 pad 16: (no net) -> Net-(U17-Pad16)
- U17 pad 8: (no net) -> Net-(U17-Pad8)
- U18 pad 16: (no net) -> Net-(U18-Pad16)
- U18 pad 8: (no net) -> Net-(U18-Pad8)
- U19 pad 16: (no net) -> Net-(U19-Pad16)
- U19 pad 8: (no net) -> Net-(U19-Pad8)
- U20 pad 16: (no net) -> Net-(U20-Pad16)
- U20 pad 8: (no net) -> Net-(U20-Pad8)
- U21 pad 16: (no net) -> Net-(U21-Pad16)
- U21 pad 8: (no net) -> Net-(U21-Pad8)
- U22 pad 16: (no net) -> Net-(U22-Pad16)
- U22 pad 8: (no net) -> Net-(U22-Pad8)
- U23 pad 10: (no net) -> Net-(U23-Pad10)
- U24 pad 10: (no net) -> Net-(U24-Pad10)
- U25 pad 10: (no net) -> Net-(U25-Pad10)
- U26 pad 10: (no net) -> Net-(U26-Pad10)
- U27 pad 10: (no net) -> Net-(U27-Pad10)
- U28 pad 10: (no net) -> Net-(U28-Pad10)
- U29 pad 10: (no net) -> Net-(U29-Pad10)
- U3 pad 15: LEDOE -> I2S_DIN1
- U3 pad 20: (no net) -> Net-(U3-Pad20)
- U3 pad 26: (no net) -> SD_LED_SCK
- U3 pad 29: SD_LED_SCK -> Net-(U3-Pad29)
- U3 pad 30: SD_LED_MOSI -> I2S_DOUT1
- U3 pad 31: (no net) -> SD_LED_MOSI
- U3 pad 32: (no net) -> Net-(U3-Pad32)
- U3 pad 33: (no net) -> Net-(U3-Pad33)
- U3 pad 35: (no net) -> Net-(U3-Pad35)
- U3 pad 37: (no net) -> Net-(U3-Pad37)
- U3 pad 38: (no net) -> Net-(U3-Pad38)
- U3 pad 41: (no net) -> Net-(U3-Pad41)
- U3 pad 48: (no net) -> Net-(U3-Pad48)
- U3 pad 49: (no net) -> Net-(U3-Pad49)
- U3 pad 6: (no net) -> LEDOE
- U3 pad 7: (no net) -> Net-(U3-Pad7)
- U3 pad 8: (no net) -> Net-(U3-Pad8)
- U30 pad 10: (no net) -> Net-(U30-Pad10)
- U30 pad 9: (no net) -> Net-(U30-Pad9)
- U5 pad 11: (no net) -> Net-(U5-Pad11)
- U5 pad 12: (no net) -> Net-(U5-Pad12)
- U5 pad 13: (no net) -> Net-(U5-Pad13)
- U5 pad 14: (no net) -> Net-(U5-Pad14)
- U5 pad 15: (no net) -> Net-(U5-Pad15)
- U5 pad 16: (no net) -> Net-(U5-Pad16)
- U5 pad 18: (no net) -> Net-(U5-Pad18)
- U6 pad 1: (no net) -> Net-(U6-Pad1)
- U6 pad 10: (no net) -> Net-(U6-Pad10)
- U6 pad 11: (no net) -> Net-(U6-Pad11)
- U6 pad 12: (no net) -> Net-(U6-Pad12)
- U6 pad 8: (no net) -> Net-(U6-Pad8)
- U6 pad 9: (no net) -> Net-(U6-Pad9)
- U7 pad 10: (no net) -> Net-(U7-Pad10)
- U7 pad 9: (no net) -> Net-(U7-Pad9)
- U8 pad 10: (no net) -> Net-(U8-Pad10)
- U8 pad 14: (no net) -> Net-(U8-Pad14)
- U8 pad 9: (no net) -> Net-(U8-Pad9)
